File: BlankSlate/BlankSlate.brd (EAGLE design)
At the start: 36.3 x 29.8 mm, 32 parts, among them U1 ATTINY48/88-TQFP

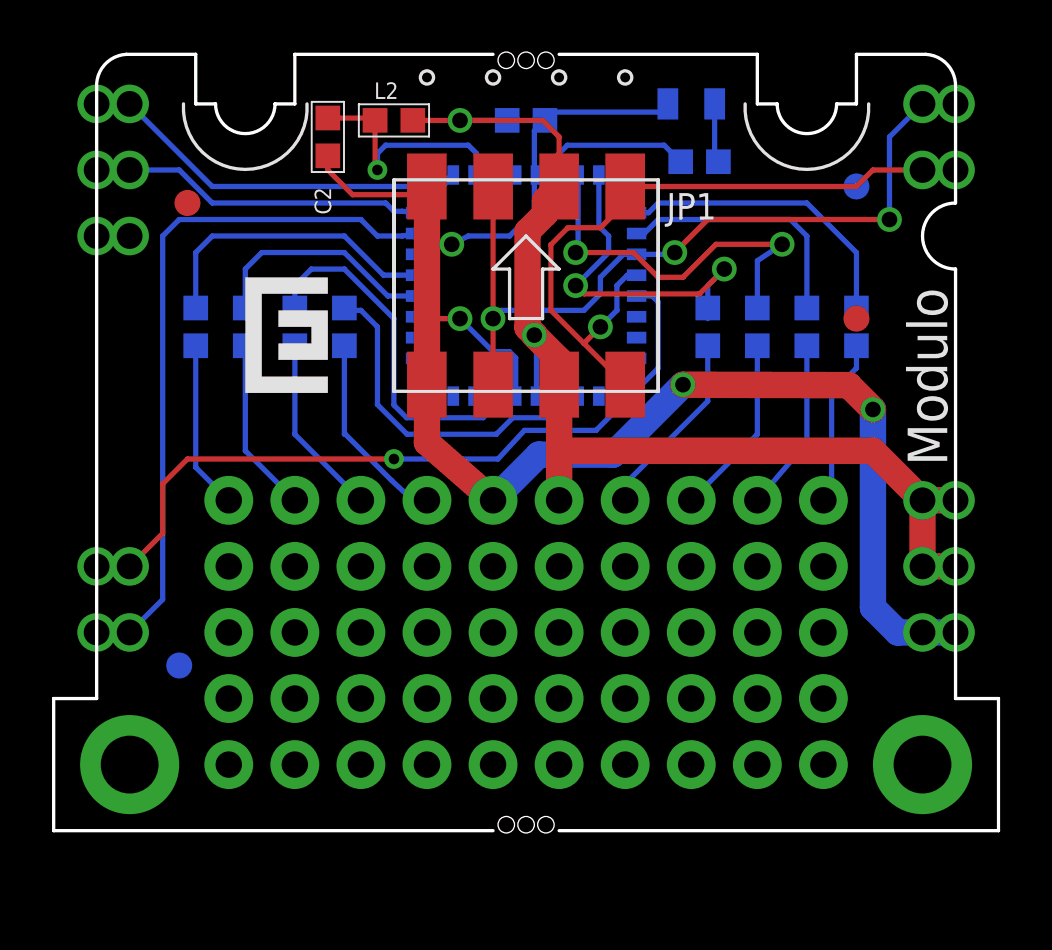
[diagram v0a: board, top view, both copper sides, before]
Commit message: Check point of current PCB designs. Among other things I think this change includes rewiring of programming lines on many of the boards,.
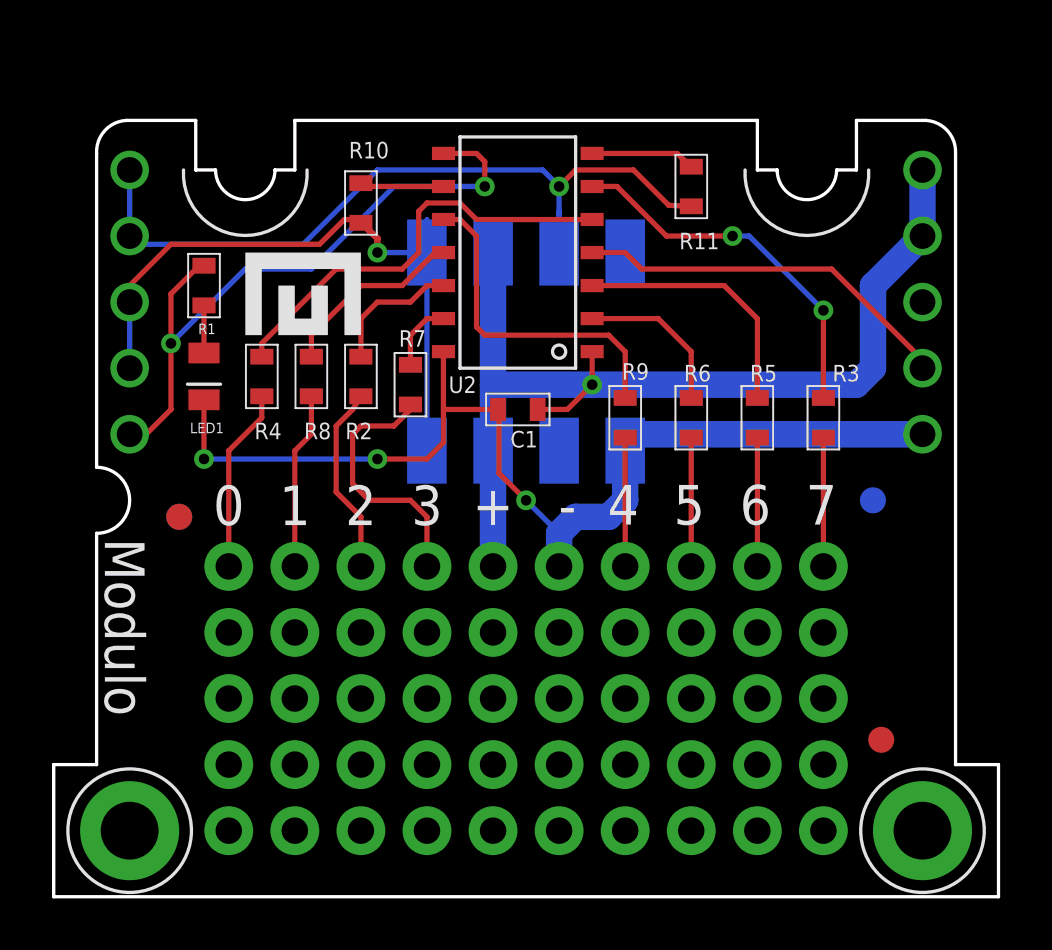
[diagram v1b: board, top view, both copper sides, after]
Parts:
- removed C2: .1uF, Modulo:0603
- removed L2: 10uH, Modulo:0603
- removed U1: ATTINY48/88-TQFP, Modulo:TQFP-32
- added R10, R11: 150Ω, Modulo:0603
- added U2: ATTINY841, Modulo:SOIC-14
- PCB1: value DEVICE-PCB-TABS -> DEVICE-PCB; device Modulo:DEVICE-PCB-TABS -> Modulo:DEVICE-PCB
- moved FID2 29.0 mm to (4.45, 14.6), flipped to the top
- moved FID4 28.7 mm to (31.1, 15.2), flipped to the bottom
- moved FID1 27.1 mm to (31.4, 6.03), flipped to the top
- moved FID5 27.1 mm to (4.45, 14.6), flipped to the bottom
- moved LED1 21.5 mm to (5.40, 20.0), flipped to the top, turned to 180 degrees
- moved R1 19.6 mm to (5.40, 23.5), flipped to the top, turned to 90 degrees
- moved R2 19.1 mm to (11.4, 20.0), flipped to the top
- moved R4 19.1 mm to (7.62, 20.0), flipped to the top
- moved JP2 18.0 mm to (11.4, 12.7), flipped to the bottom
- moved JP4 18.0 mm to (6.35, 12.7), flipped to the bottom
- moved PCB1 17.8 mm to (0.00, 0.00)
- moved R9 16.9 mm to (21.6, 18.4), flipped to the top
- moved JP9 15.5 mm to (21.6, 12.7), flipped to the bottom
- moved R6 13.8 mm to (24.1, 18.4), flipped to the top
- moved C1 11.1 mm to (17.5, 18.7), flipped to the top
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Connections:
- removed net LED: R1.2, U1.22
- removed net MISO: PCB1.MISO, PCB1.MISO1, U1.16
- removed net MOSI: PCB1.MOSI, PCB1.MOSI1, U1.15
- removed net N$5 (its old number): C2.2, L2.1, U1.18
- removed net SCK: PCB1.CLK, PCB1.CLK1, U1.17
- new net MISO/LED: PCB1.MISO, R1.2, U2.8
- new net SCL/SCK: R10.2, U2.9
- new net SDA/MOSI: R11.2, U2.7
- net GND: now also U2.14; no longer C2.1, PCB1.GND1, U1.21, U1.5
- net IO0: now also R4.1, U2.5; no longer R2.1, U1.25
- net IO1: now also R8.1, U2.11; no longer R3.1, U1.26
- net IO2: now also R2.1, U2.12; no longer R4.1, U1.23
- net IO3: now also R7.1, U2.13; no longer R5.1, U1.24
- net IO4: now also R9.1, U2.10; no longer R6.1, U1.3
- net IO5: now also R6.1, U2.2; no longer R7.1, U1.6
- net IO6: now also R5.1, U2.3; no longer R8.1, U1.12
- net IO7: now also R3.1, U2.6; no longer R9.1, U1.13
- net RESET: now also U2.4; no longer PCB1.RESET1, U1.29
- net SCL: now also PCB1.CLK, R10.1; no longer PCB1.SCL1, U1.28
- net SDA: now also PCB1.MOSI, R11.1; no longer PCB1.SDA1, U1.27
- net VCC: now also U2.1; no longer L2.2, PCB1.VCC1, PCB1.VPROG1, U1.4
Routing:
- net MOSI: track 27.3 -> 0.00 mm
- net MISO/LED: track 0.00 -> 25.4 mm, vias 0 -> 2
- net GND: track 66.1 -> 41.4 mm, vias 4 -> 3
- net SCK: track 15.3 -> 0.00 mm
- net RESET: track 29.4 -> 14.7 mm, vias 1 -> 0
- net MISO: track 12.9 -> 0.00 mm
- net IO3: track 13.3 -> 2.68 mm, vias 2 -> 0
- net IO2: track 14.8 -> 5.16 mm, vias 2 -> 0
- net N$5 (its old number): track 9.45 -> 0.00 mm, vias 1 -> 0
- net IO5: track 13.7 -> 6.11 mm
- net LED: track 5.93 -> 0.00 mm
- net IO0: track 11.5 -> 16.6 mm
- net VCC: track 45.8 -> 40.8 mm, vias 2 -> 1
- net SDA/MOSI: track 0.00 -> 4.01 mm
- net SCL/SCK: track 0.00 -> 3.23 mm
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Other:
- outline, holes or cut-outs redrawn

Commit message: Added 3.3V regulator and solder jump to select operating voltage 10mil traces instead of 8 swapped I/O pins 3 and 4 so that PWM capable pins are contiguous moved the status LED so that it's next to the logo bumped version number to 4
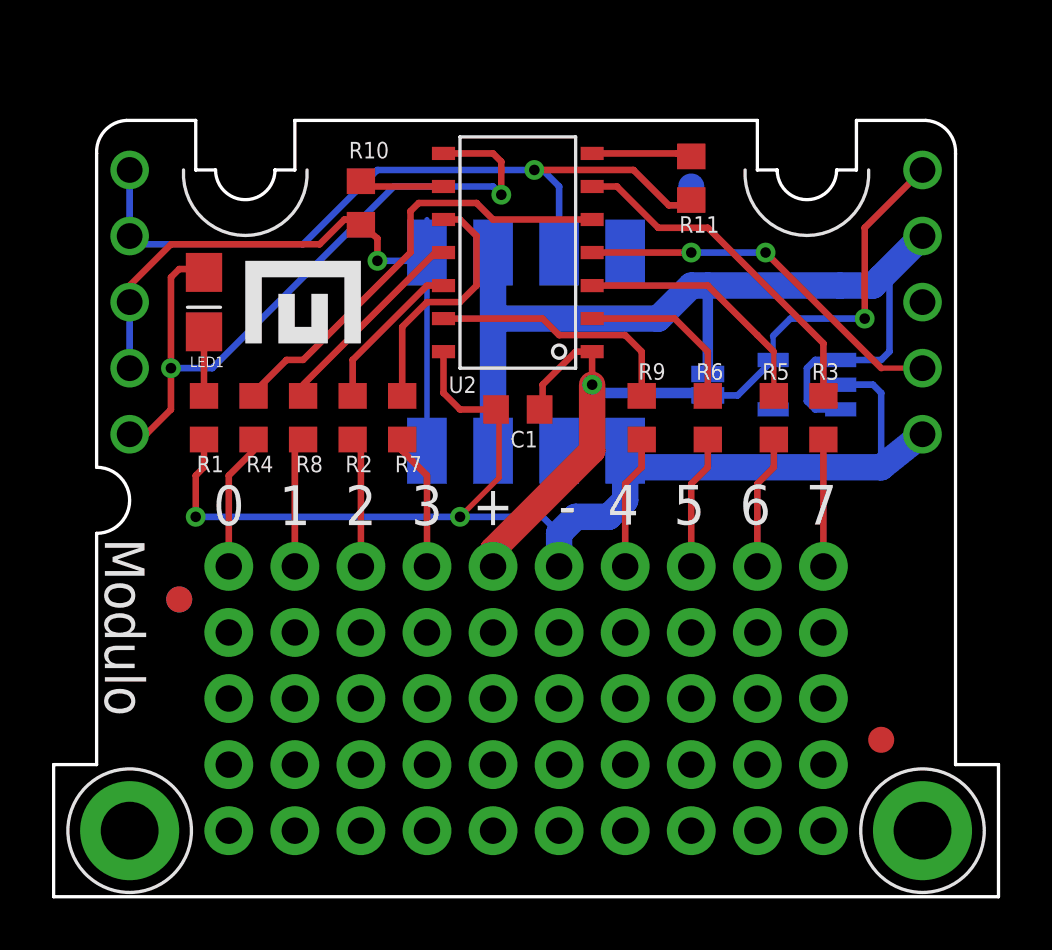
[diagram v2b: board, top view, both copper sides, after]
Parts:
- added SJ1: SOLDERJUMPERNC, SparkFun-Passives:SJ_2S
- added U1: MIC5205-3.3YM5 TR, Modulo:SOT23-5
- moved FID4 13.9 mm to (24.1, 27.3)
- moved R1 5.08 mm to (5.40, 18.4)
- moved FID2 3.18 mm to (4.45, 11.4)
- moved FID5 3.18 mm to (4.45, 11.4)
- moved LED1 2.86 mm to (5.40, 22.9)
- moved R8 1.62 mm to (9.21, 18.4)
- moved R2 1.62 mm to (11.1, 18.4)
- moved R4 1.62 mm to (7.30, 18.4)
- moved R7 1.31 mm to (13.0, 18.4)
- moved R6 0.64 mm to (24.8, 18.4)
- moved R9 0.64 mm to (22.2, 18.4)
- moved U$1 0.63 mm to (8.57, 19.1)
- moved R5 0.63 mm to (27.3, 18.4)
- moved U$2 0.32 mm to (8.89, 21.9)
- moved R11 0.32 mm to (24.1, 27.6)
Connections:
- removed net N$2: LED1.A, R1.1
- new net N$10: LED1.C, R1.2
- new net VIN: JP1.P$5, JP1.P$6, PCB1.VCC, SJ1.1, U1.1, U1.3
- net GND: now also R1.1, U1.2; no longer LED1.C
- net IO3: now also U2.10; no longer U2.13
- net IO4: now also U2.13; no longer U2.10
- net MISO/LED: now also LED1.A; no longer R1.2
- net VCC: now also SJ1.2, U1.5; no longer JP1.P$5, JP1.P$6, PCB1.VCC
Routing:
- net VIN: track 0.00 -> 39.4 mm
- net GND: track 41.4 -> 50.4 mm, vias 3 -> 2
- net VCC: track 40.8 -> 32.3 mm, vias 1 -> 2
- net IO3: track 2.68 -> 9.61 mm
- net N$5: track 10.0 -> 5.27 mm
- net IO4: track 12.9 -> 9.85 mm
- net MISO/LED: track 25.4 -> 27.9 mm
- net N$10: track 0.00 -> 2.46 mm
- net N$6: track 7.29 -> 5.41 mm
- net N$2: track 1.83 -> 0.00 mm
- net N$3: track 7.07 -> 5.27 mm
- net N$12: track 6.80 -> 5.01 mm
- net IO2: track 5.16 -> 6.06 mm
- net IO7: track 14.2 -> 13.4 mm, vias 2 -> 0
- net SDA: track 30.7 -> 29.9 mm
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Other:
- board text added: "closed: 5V open: 3.3V"

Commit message: Fixed PARTNUM on 3.3v regulator.
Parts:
- U1: value MIC5205-3.3YM5 TR -> VREG-MIC5205-3.3V
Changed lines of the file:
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@@
 <attribute name="VALUE" x="21.209" y="16.0655" size="0.635" layer="27" font="vector"/>
 </element>
-<element name="U1" library="Modulo" package="SOT23-5" value="MIC5205-3.3YM5 TR" x="28.575" y="19.685" smashed="yes" rot="MR270">
+<element name="U1" library="Modulo" package="SOT23-5" value="VREG-MIC5205-3.3V" x="28.575" y="19.685" smashed="yes" rot="MR270">
 <attribute name="NAME" x="28.0035" y="21.971" size="0.4064" layer="26" rot="MR180"/>
+<attribute name="PARTNUM" value="MIC5205-3.3YM5 TR" x="28.575" y="19.685" size="1.778" layer="28" rot="MR270" display="off"/>
 </element>
 <element name="SJ1" library="SparkFun-Passives" package="SJ_2S" value="SOLDERJUMPERNC" x="24.765" y="19.685" smashed="yes" rot="MR270">

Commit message: Various small tweaks based on testing and feedback from manufacturer.
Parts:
- R10, R11: value 150Ω -> 0Ω
- SJ1: value SOLDERJUMPERNC -> SOLDERJUMPERNO; device SparkFun-Passives:SJ_2S -> SparkFun-Passives:SJ_2S-NO
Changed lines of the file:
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@@
 <attribute name="NAME" x="15.875" y="20.0025" size="0.635" layer="25" rot="R180"/>
 </element>
-<element name="R10" library="Modulo" package="0603" value="150Ω" x="11.43" y="26.67" smashed="yes" rot="R90">
-<attribute name="PARTNUM" value="ERJ-3EKF1500V" x="6.985" y="26.67" size="1.778" layer="27" rot="R90" display="off"/>
+<element name="R10" library="Modulo" package="0603" value="0Ω" x="11.43" y="26.67" smashed="yes" rot="R90">
+<attribute name="PARTNUM" value="ERJ-3GEY0R00V" x="6.985" y="26.67" size="1.778" layer="27" rot="R90" display="off"/>
 <attribute name="NAME" x="12.5095" y="29.0195" size="0.635" layer="25" font="vector" rot="R180"/>
-<attribute name="VALUE" x="12.2555" y="27.686" size="0.635" layer="27" font="vector" rot="R270"/>
-</element>
-<element name="R11" library="Modulo" package="0603" value="150Ω" x="24.13" y="27.6225" smashed="yes" rot="R90">
-<attribute name="PARTNUM" value="ERJ-3EKF1500V" x="23.495" y="24.4475" size="1.778" layer="27" rot="R90" display="off"/>
+<attribute name="VALUE" value="0Ω" x="12.2555" y="27.686" size="0.635" layer="27" font="vector" rot="R270"/>
+</element>
+<element name="R11" library="Modulo" package="0603" value="0Ω" x="24.13" y="27.6225" smashed="yes" rot="R90">
+<attribute name="PARTNUM" value="ERJ-3GEY0R00V" x="23.495" y="24.4475" size="1.778" layer="27" rot="R90" display="off"/>
 <attribute name="NAME" x="25.2095" y="26.162" size="0.635" layer="25" font="vector" rot="R180"/>
-<attribute name="VALUE" x="25.4635" y="29.972" size="0.635" layer="27" font="vector" rot="R180"/>
+<attribute name="VALUE" value="0Ω" x="25.4635" y="29.972" size="0.635" layer="27" font="vector" rot="R180"/>
 </element>
 <element name="R7" library="Modulo" package="0603" value="150Ω" x="13.0175" y="18.415" smashed="yes" rot="R270">
@@
 <attribute name="PARTNUM" value="MIC5205-3.3YM5 TR" x="28.575" y="19.685" size="1.778" layer="28" rot="MR270" display="off"/>
 </element>
-<element name="SJ1" library="SparkFun-Passives" package="SJ_2S" value="SOLDERJUMPERNC" x="24.765" y="19.685" smashed="yes" rot="MR270">
+<element name="SJ1" library="SparkFun-Passives" package="SJ_2S-NO" value="SOLDERJUMPERNO" x="24.765" y="19.685" smashed="yes" rot="MR270">
 <attribute name="BOM" value="EXCLUDE" x="24.765" y="19.685" size="1.778" layer="28" rot="MR270" display="off"/>
 <attribute name="NAME" x="24.1327" y="21.59" size="0.4064" layer="26" rot="MR180"/>
@@
 <wire x1="28.8925" y1="20.6375" x2="29.2376" y2="20.6375" width="0.254" layer="16"/>
 <wire x1="29.2376" y1="20.6375" x2="29.8751" y2="20.635" width="0.2032" layer="16"/>
-<wire x1="24.765" y1="20.0969" x2="24.765" y2="23.495" width="0.4064" layer="16"/>
+<wire x1="24.765" y1="20.135" x2="24.765" y2="23.495" width="0.4064" layer="16"/>
 <wire x1="29.8751" y1="20.635" x2="31.43" y2="20.635" width="0.254" layer="16"/>
 <wire x1="31.43" y1="20.635" x2="31.75" y2="20.955" width="0.254" layer="16"/>
@@
 <contactref element="U1" pad="5"/>
 <contactref element="C1" pad="1"/>
-<wire x1="24.765" y1="19.2731" x2="25.913" y2="19.2731" width="0.254" layer="16"/>
+<wire x1="24.765" y1="19.235" x2="25.913" y2="19.2731" width="0.254" layer="16"/>
 <wire x1="25.913" y1="19.2731" x2="27.2749" y2="20.635" width="0.254" layer="16"/>
 <via x="20.32" y="19.685" extent="1-16" drill="0.4064"/>
@@
 <wire x1="20.32" y1="19.685" x2="20.6375" y2="19.3675" width="0.4064" layer="16"/>
 <wire x1="20.6375" y1="19.3675" x2="24.4475" y2="19.3675" width="0.4064" layer="16"/>
-<wire x1="24.4475" y1="19.3675" x2="24.765" y2="19.2731" width="0.4064" layer="16"/>
+<wire x1="24.4475" y1="19.3675" x2="24.765" y2="19.235" width="0.4064" layer="16"/>
 <wire x1="18.415" y1="19.685" x2="18.415" y2="18.8468" width="0.254" layer="1"/>
 <wire x1="18.415" y1="18.8468" x2="18.3007" y2="18.7325" width="0.2032" layer="1"/>

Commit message: Added unique board prefixes to part numbers due to CM requirements
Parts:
- renumbered C1 to 8-C1, JP1 to 8-JP1, LED1 to 8-LED1, PCB1 to 8-PCB1, R1 to 8-R1, R10 to 8-R10, R11 to 8-R11, R2 to 8-R2, R3 to 8-R3, R4 to 8-R4, R5 to 8-R5, R6 to 8-R6, R7 to 8-R7, R8 to 8-R8, R9 to 8-R9, SJ1 to 8-SJ1, U1 to 8-U1, U2 to 8-U2
